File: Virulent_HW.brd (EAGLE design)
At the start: 100 x 80 mm, 76 parts, among them SW1 COM08229, SW2 COM08720, U1 STM32F050G6U6

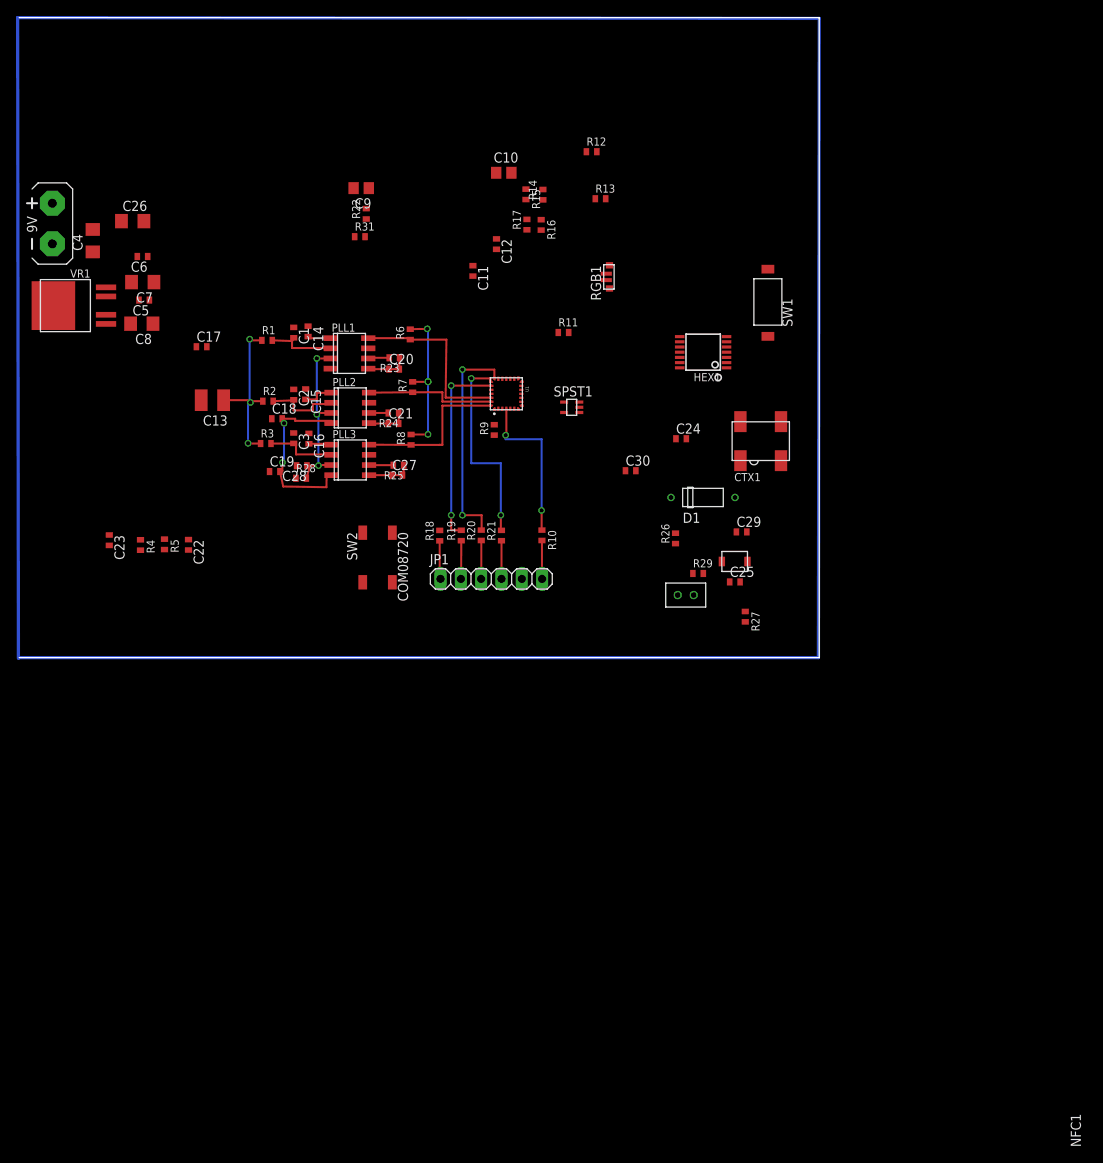
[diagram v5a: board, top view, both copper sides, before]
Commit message: First Draft of PCB. Changes made to reciever of schematic per Nic's instructions.Changed LED pins to better suit routing needs. Added dpdt switch to change nfc coil from tx/rx, to be controlled by microcontroller. Added user's momentary push-button
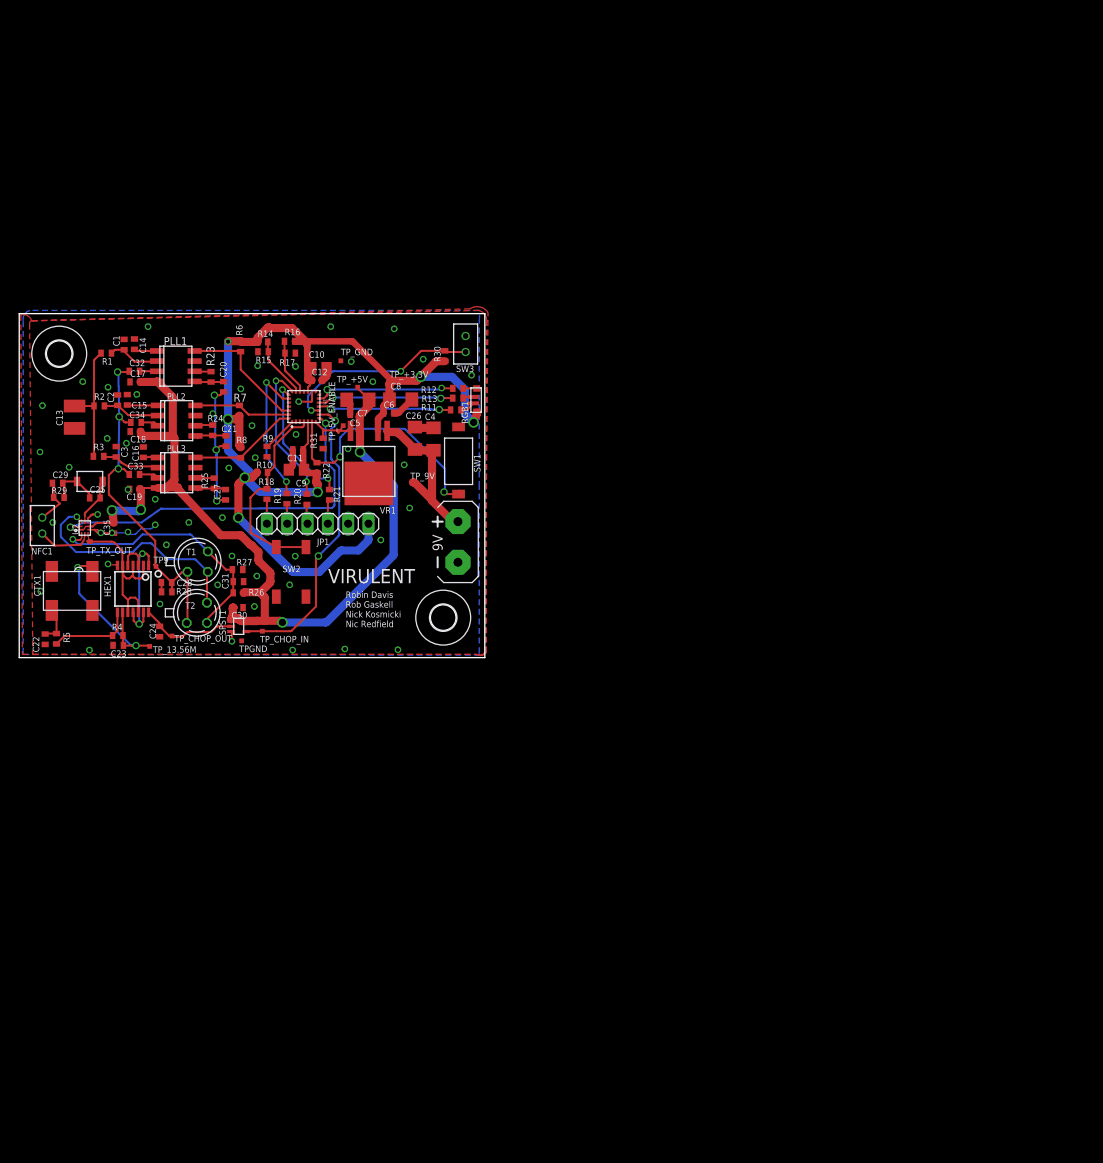
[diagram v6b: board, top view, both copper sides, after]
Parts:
- removed D1: NTE583, Virulent_HW:NTE583
- added C31, C35: 1n, rcl:C0402
- added C32, C33, C34: 470n, rcl:C0402
- added H1, H2: MOUNT-HOLE3.2, holes:3,2
- added R30: 10k, Virulent_HW:R0402
- added SW3: BUTTON, Virulent_HW:17M2-G
- added T1, T2: (no value), transistor:TO18
- added TP9, TPGND, TP_+3.3V, TP_+5V, TP_13.56M, TP_5V_ENABLE, TP_9V, TP_CHOP_IN, TP_CHOP_OUT, TP_GND, TP_TX_OUT: TPTP06SQ, testpad:TP06SQ
- added U2: MAX14536, Virulent_HW:10UTQFN
- R26: value 1Meg -> 150k
- R27: value 5.6Meg -> 100k
- moved CTX1 88.1 mm to (6.61, 8.34), turned to 180 degrees
- moved C29 85.7 mm to (4.80, 21.8)
- moved CT1 81.2 mm to (8.83, 22.0)
- moved NFC1 80.9 mm to (2.88, 16.5), turned to 180 degrees
- moved C25 80.7 mm to (9.46, 20.0)
- moved R29 80.5 mm to (4.96, 20.0)
- moved HEX1 77.6 mm to (13.9, 8.59), turned to 180 degrees
- moved C24 69.5 mm to (17.6, 3.26), turned to 270 degrees
- moved G1 64.5 mm to (54.8, 14.5)
- moved R27 63.7 mm to (27.3, 11.0), turned to 180 degrees
- moved R26 55.1 mm to (27.4, 8.10), turned to 0 degrees
- moved C30 52.0 mm to (27.3, 6.26)
- moved SPST1 49.8 mm to (27.4, 3.91), turned to 0 degrees
- moved C4 49.3 mm to (51.8, 27.3)
- moved C26 44.5 mm to (49.5, 27.4), turned to 270 degrees
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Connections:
- net TEAMID0 renamed N$34
- removed net LED_BLUE: R13.1, RGB1.3
- removed net LED_GREEN: R11.1, RGB1.1
- removed net LED_RED: R12.1, RGB1.2
- removed net N$11: C30.2, SPST1.5
- removed net NFC: C28.1, D1.P$1, HEX1.10, HEX1.12, HEX1.2, HEX1.4, HEX1.6, PLL1.3, PLL2.3, PLL3.3, R28.2
- removed net O_BLUE: R13.2, U1.25
- removed net O_GREEN: R11.2, U1.15
- removed net O_RED: R12.2, U1.24
- new net +2V: C31.1, R26.1, R27.2, T1.3, T2.2, U2.3
- new net N$16: C32.2, PLL1.3
- new net N$20: C25.2, CT1.2, U2.9
- new net N$21: R11.1, RGB1.3
- new net N$22: T1.2, T2.3, U2.10
- new net N$23: C34.2, PLL2.3
- new net N$25: C33.2, PLL3.3
- new net N$28: R11.2, U1.11
- new net N$31: R12.2, U1.13
- new net N$32: NFC1.1, U2.4
- new net N$35: R12.1, RGB1.1
- new net N$36: R13.1, RGB1.2
- new net RX_OUT: C28.1, C32.1, C33.1, C34.1, R28.2, T1.1, T2.1, TP9.TP
- new net TRIGGER: R30.1, SW3.2, U1.10
- new net TX/RX: U1.8, U2.1
- new net TX_OUT: HEX1.10, HEX1.12, HEX1.2, HEX1.4, HEX1.6, TP_TX_OUT.TP, U2.5
- net +3.3V: now also R30.2, TP_+3.3V.TP
- net +5V: now also C35.2, R26.2, SPST1.5, TP_+5V.TP, U2.2, U2.7; no longer R27.2
- net +9-36V: now also TP_9V.TP
- net 5V_ENABLE: now also TP_5V_ENABLE.TP
- net CHOPPED_FREQ: now also TP_CHOP_OUT.TP
- net GND: now also C30.2, C31.2, C35.1, R27.1, SW3.1, TPGND.TP, TP_GND.TP, U2.6, U2.8; no longer C25.2, CT1.2, R26.1
- net MOD_FREQ: now also TP_CHOP_IN.TP
- net N$18: now also TP_13.56M.TP
- net N$29: now also R13.2, U1.12; no longer D1.P$2, NFC1.1, R26.2, R27.1
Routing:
- net GND: track 360.1 -> 50.3 mm, vias 0 -> 56
- net +3.3V: track 24.5 -> 138.9 mm, vias 4 -> 7
- net +5V: track 23.4 -> 117.2 mm, vias 2 -> 4
- net TX/RX: track 0.00 -> 46.9 mm, vias 0 -> 2
- net RX_OUT: track 0.00 -> 46.0 mm, vias 0 -> 3
- net MOD_FREQ: track 0.00 -> 37.3 mm, vias 0 -> 2
- net +2V: track 0.00 -> 32.6 mm, vias 0 -> 1
- net NRESET_SOFT: track 0.02 -> 31.9 mm, vias 0 -> 2
- net N$22: track 0.00 -> 29.7 mm, vias 0 -> 1
- net TRIGGER: track 0.00 -> 25.0 mm, vias 0 -> 2
- net TX_OUT: track 0.00 -> 23.8 mm
- net N$18: track 0.00 -> 23.4 mm, vias 0 -> 2
- net NFC: track 22.1 -> 0.00 mm, vias 3 -> 0
- net +9-36V: track 0.00 -> 20.8 mm
- net N$24: track 0.00 -> 19.4 mm, vias 0 -> 2
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- added copper zone on layer 1, net GND
- added copper zone on layer 16, net GND
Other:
- board size 100 x 80 mm -> 58.2 x 43 mm
- board text added: "Robin Davis Rob Gaskell Nick Kosmicki Nic Redfield"
- board text added: "VIRULENT"

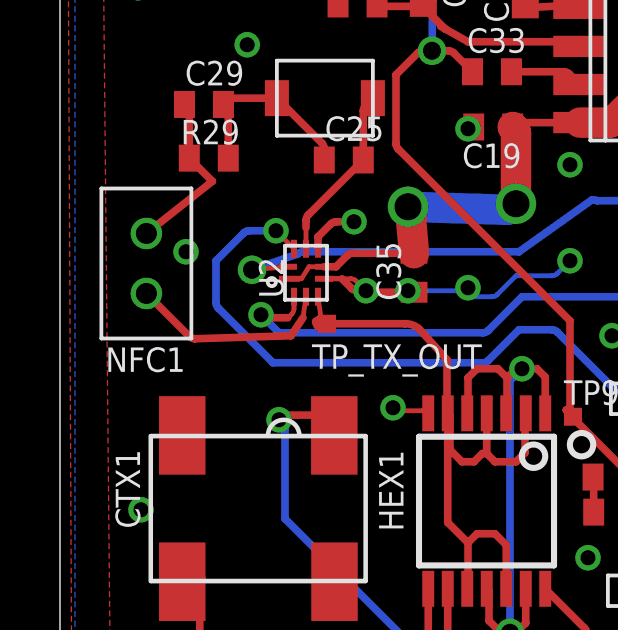
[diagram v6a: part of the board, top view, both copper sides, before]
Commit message: minor changes made to schematic for primarily esthetic reasons. Changed Version number to 2.0
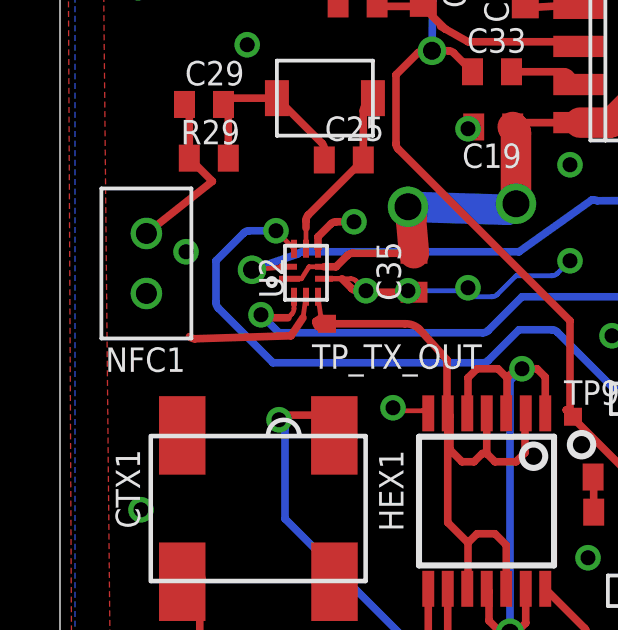
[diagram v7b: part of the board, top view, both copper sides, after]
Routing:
- net N$32: track 6.86 -> 4.83 mm
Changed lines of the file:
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@@
 </signal>
 <signal name="N$32">
-<contactref element="NFC1" pad="1"/>
 <contactref element="U2" pad="4"/>
 <wire x1="8.2" y1="15.4" x2="8.1" y2="14.7" width="0.16" layer="1"/>
@@
 <wire x1="7.7" y1="14.1" x2="4.495209375" y2="14" width="0.254" layer="1"/>
 <wire x1="4.495209375" y1="14" x2="4.31560625" y2="14.07439375" width="0.254" layer="1" curve="-44.999502"/>
-<wire x1="4.31560625" y1="14.07439375" x2="2.88" y2="15.51" width="0.254" layer="1"/>
+<contactref element="NFC1" pad="1"/>
+<wire x1="4.31560625" y1="14.07439375" x2="2.88" y2="15.51" width="0" layer="19" extent="1-1"/>
 </signal>
 <signal name="N$33">

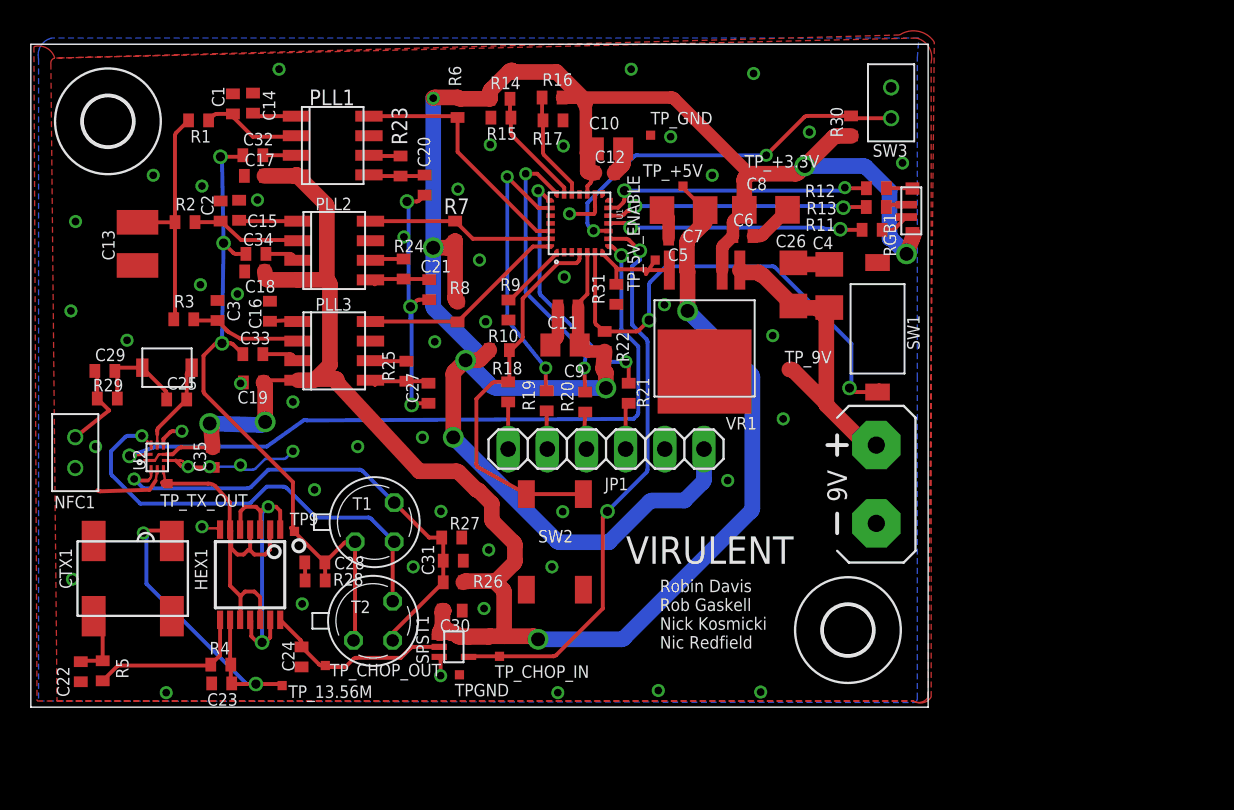
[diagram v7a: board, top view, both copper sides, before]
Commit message: Moved LDO, resized vias.
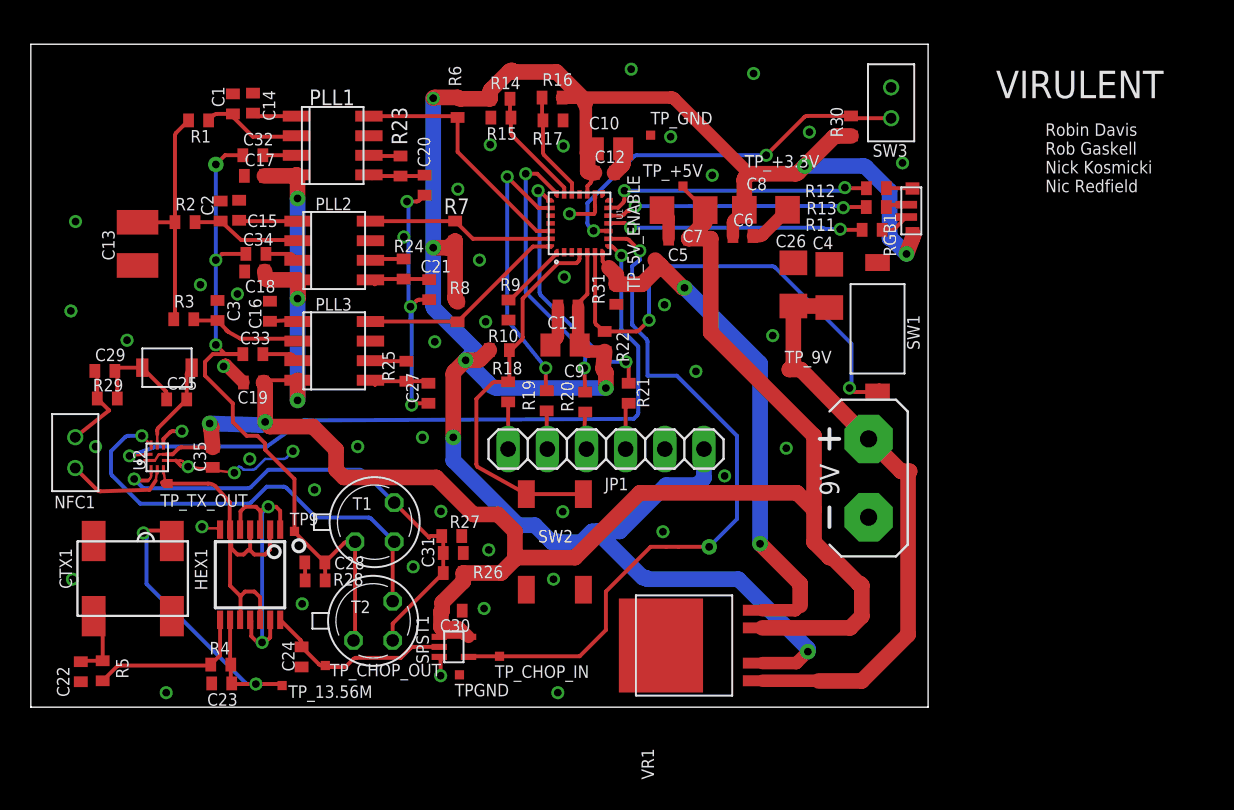
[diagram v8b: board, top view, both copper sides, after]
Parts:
- removed H1, H2: MOUNT-HOLE3.2, holes:3,2
- moved VR1 19.3 mm to (42.4, 4.00), turned to 90 degrees
- moved G1 0.64 mm to (54.3, 14.9)
- moved R26 0.60 mm to (27.4, 8.70)
- moved C31 0.50 mm to (27.4, 10.0)
- moved R27 0.10 mm to (27.3, 11.1)
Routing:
- net 5V_ENABLE: track 7.30 -> 34.7 mm, vias 0 -> 2
- net +3.3V: track 138.9 -> 157.7 mm, vias 7 -> 8
- net +9-36V: track 20.8 -> 38.5 mm
- net +5V: track 117.2 -> 133.5 mm, vias 4 -> 5
- net MOD_FREQ: track 37.3 -> 46.5 mm
- net N$32: track 4.83 -> 6.86 mm
- net RX_OUT: track 46.0 -> 47.6 mm
- net GND: vias 56 -> 51
- removed copper zone on layer 1, net GND
- removed copper zone on layer 16, net GND
